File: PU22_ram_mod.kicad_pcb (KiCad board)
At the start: 2 copper layers, 39.2 x 94.7 mm, 11 parts, among them J1 MOBO, J2 BA8, J3 BA10

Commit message: Tweaked traces a bit
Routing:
- net /D25: track 96.8 -> 91.1 mm
- net /D26: track 97.5 -> 92.2 mm
- net /D27: track 98.2 -> 93.7 mm
- net /D28: track 93.0 -> 89.6 mm
- net /D29: track 92.0 -> 89.5 mm
- net /D30: track 91.3 -> 89.4 mm
- net /D3: track 94.5 -> 94.0 mm

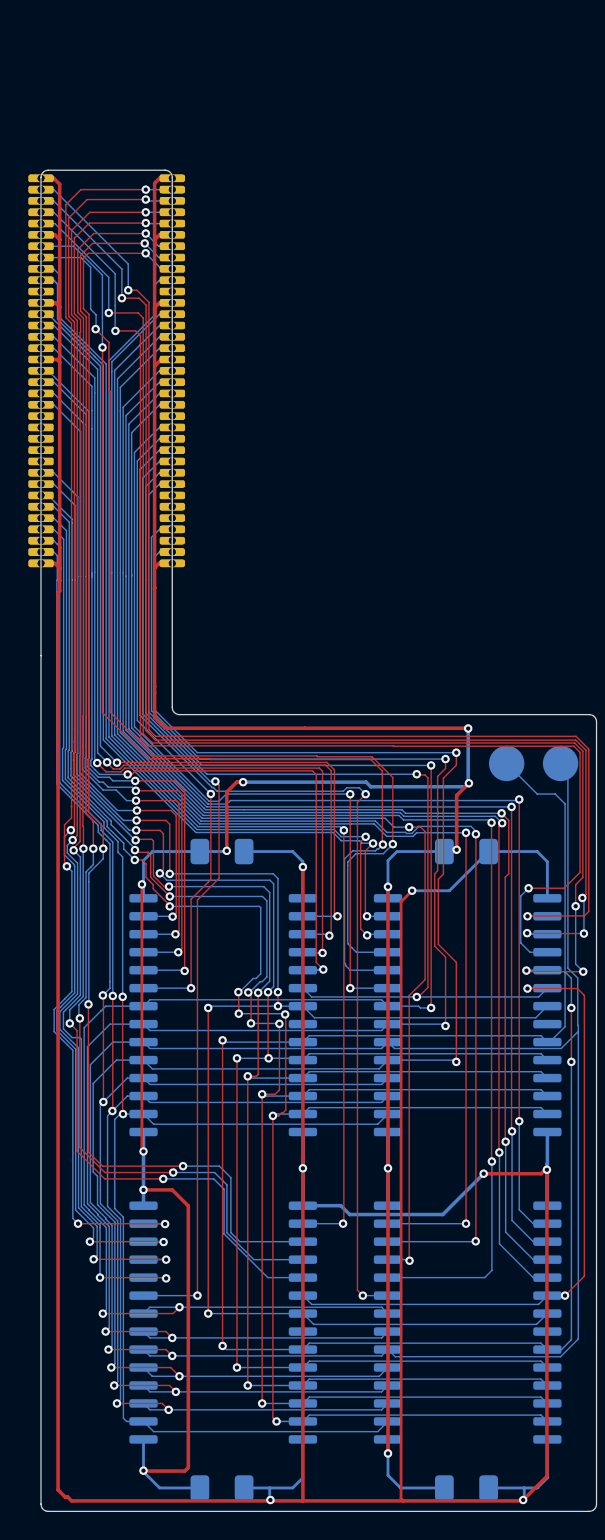
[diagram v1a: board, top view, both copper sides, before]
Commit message: make PCB a bit longer
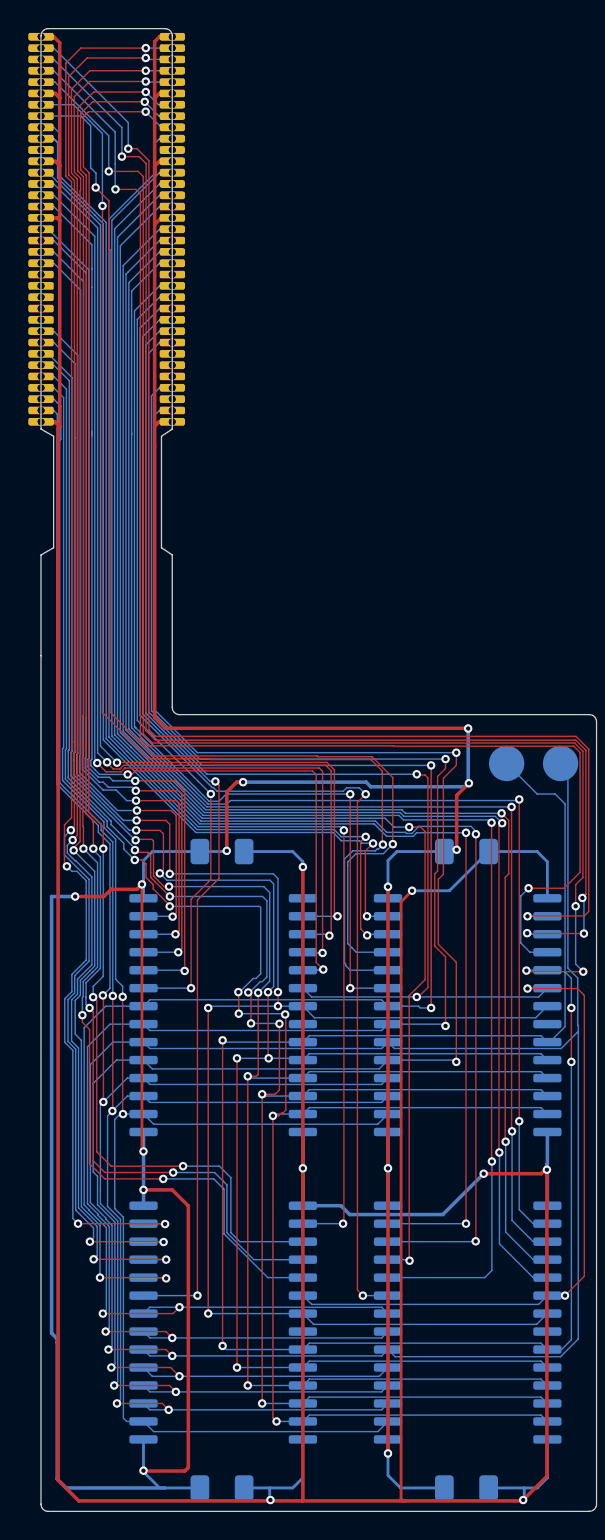
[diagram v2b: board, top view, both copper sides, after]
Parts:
- moved J1 10.0 mm to (117.0, 39.3)
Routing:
- net GND: track 224.2 -> 290.1 mm, vias 12 -> 13
- net /D31: track 89.8 -> 100.2 mm
- net /D30: track 89.4 -> 99.6 mm
- net /D29: track 89.5 -> 99.7 mm
- net /~{CAS1}: track 56.8 -> 66.9 mm
- net /D26: track 92.2 -> 102.3 mm
- net /A2: track 119.7 -> 129.8 mm
- net /D27: track 93.7 -> 103.7 mm
- net /A0: track 120.4 -> 130.4 mm
- net /~{WE}: track 120.2 -> 130.2 mm
- net /D17: track 87.2 -> 97.2 mm
- net /A6: track 105.7 -> 115.7 mm
- net /~{RAS}: track 122.1 -> 132.1 mm
- net /D3: track 94.0 -> 104.0 mm
- net /D23: track 93.3 -> 103.3 mm
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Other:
- board size 39.2 x 94.7 mm -> 39.2 x 104.7 mm

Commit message: Change outline
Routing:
- net GND: track 290.1 -> 296.2 mm, vias 13 -> 14
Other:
- board size 39.2 x 104.7 mm -> 39.1 x 104.6 mm

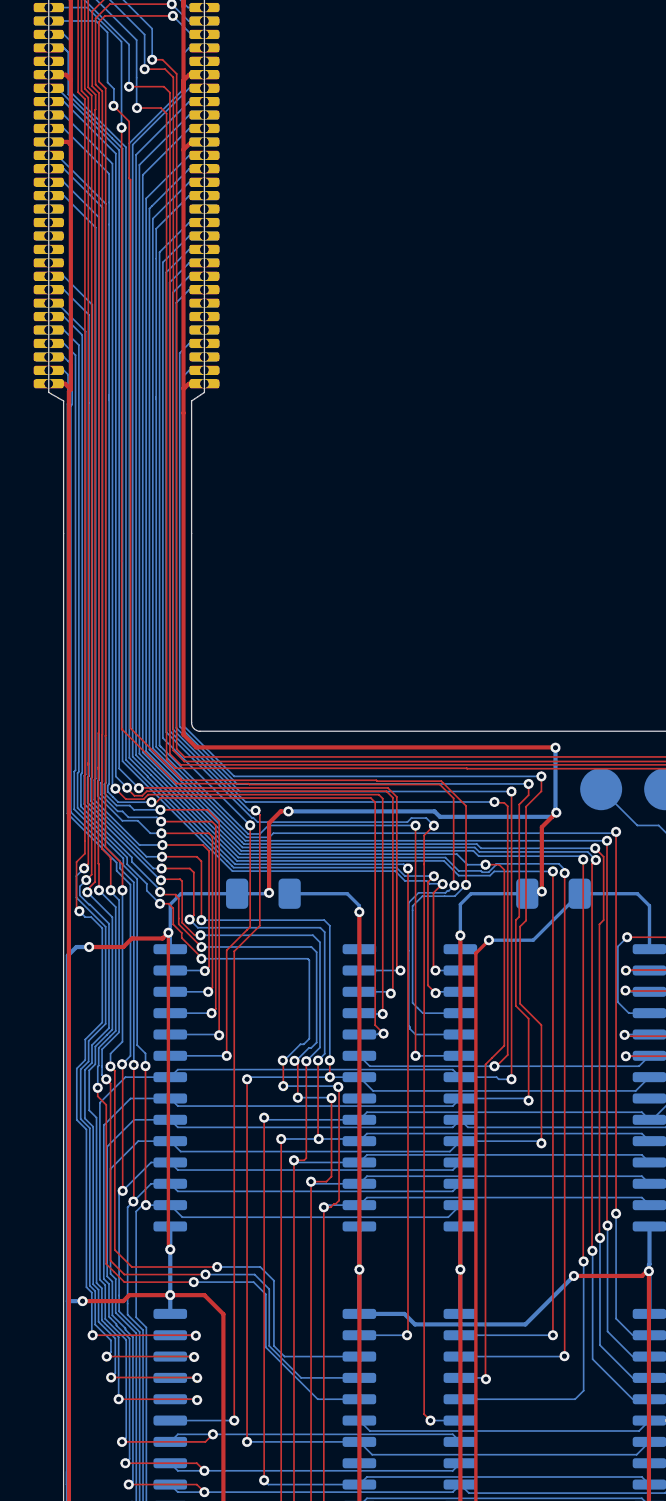
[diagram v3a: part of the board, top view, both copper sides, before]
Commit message: Reroute traces
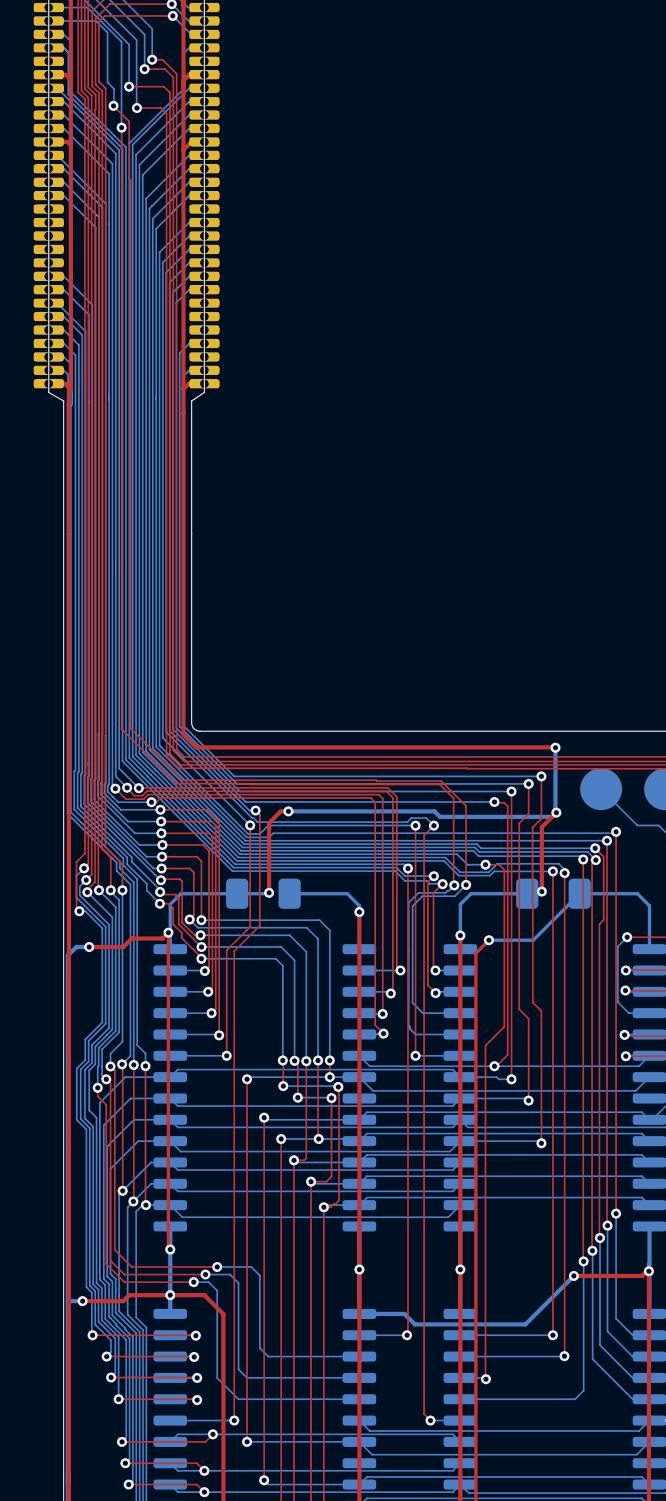
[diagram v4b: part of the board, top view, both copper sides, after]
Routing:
- net /A3: track 129.1 -> 126.5 mm
- net /A2: track 129.8 -> 127.5 mm
- net /A1: track 129.0 -> 127.5 mm
- net /D27: track 103.7 -> 104.8 mm
- net /D26: track 102.3 -> 103.3 mm
- net /A0: track 130.4 -> 129.6 mm
- net /A7: track 138.2 -> 137.6 mm

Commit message: More routing
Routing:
- net /D4: track 86.7 -> 89.2 mm
- net /D5: track 85.0 -> 86.0 mm
- net /D25: track 100.7 -> 100.2 mm

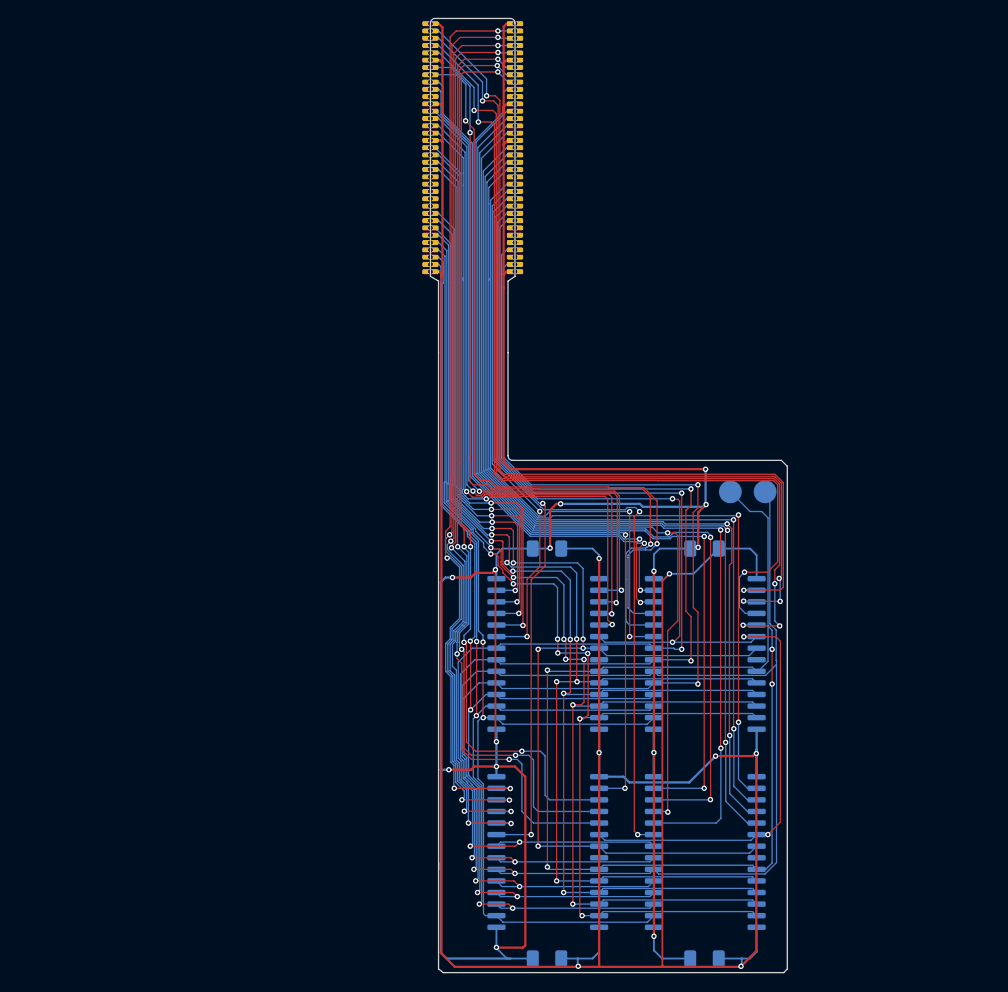
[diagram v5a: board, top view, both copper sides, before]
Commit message: Add copper fill in the zone with RAMs
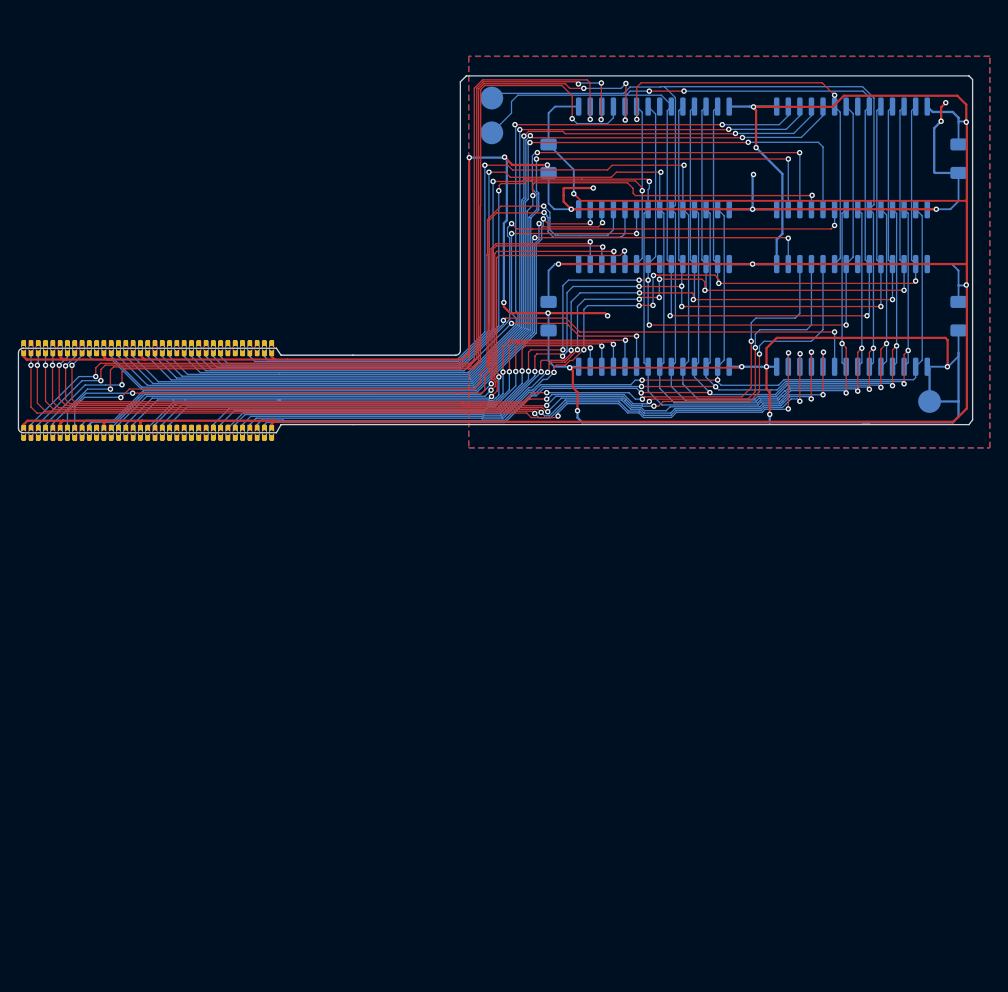
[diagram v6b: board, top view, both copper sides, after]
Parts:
- added J4: GND, TestPoint:TestPoint_Pad_D2.5mm, B.Cu at (171.7, 80.8)
- moved C2 92.0 mm to (174.9, 54.1), turned to -90 degrees
- moved C1 83.7 mm to (174.9, 71.4), turned to -90 degrees
- moved U3 73.5 mm to (154.9, 48.4), turned to -90 degrees
- moved J1 63.3 mm to (72.4, 84.2), turned to 90 degrees
- moved U4 59.5 mm to (154.9, 65.7), turned to -90 degrees
- moved U1 55.3 mm to (133.2, 48.4), turned to -90 degrees
- moved J2 52.6 mm to (123.7, 47.5), turned to -90 degrees
- moved J3 47.3 mm to (123.7, 51.3), turned to -90 degrees
- moved C4 46.0 mm to (129.9, 54.1), turned to -90 degrees
- moved U2 34.6 mm to (133.2, 65.7), turned to -90 degrees
- moved C3 25.5 mm to (129.9, 71.4), turned to -90 degrees
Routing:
- net GND: track 296.2 -> 330.6 mm, vias 14 -> 19
- net VCC: track 320.6 -> 322.5 mm
- net /D21: track 97.1 -> 97.9 mm
- added copper zone on B.Cu, net GND
- added copper zone on F.Cu, net GND
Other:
- board size 39.1 x 104.6 mm -> 104.6 x 39.1 mm

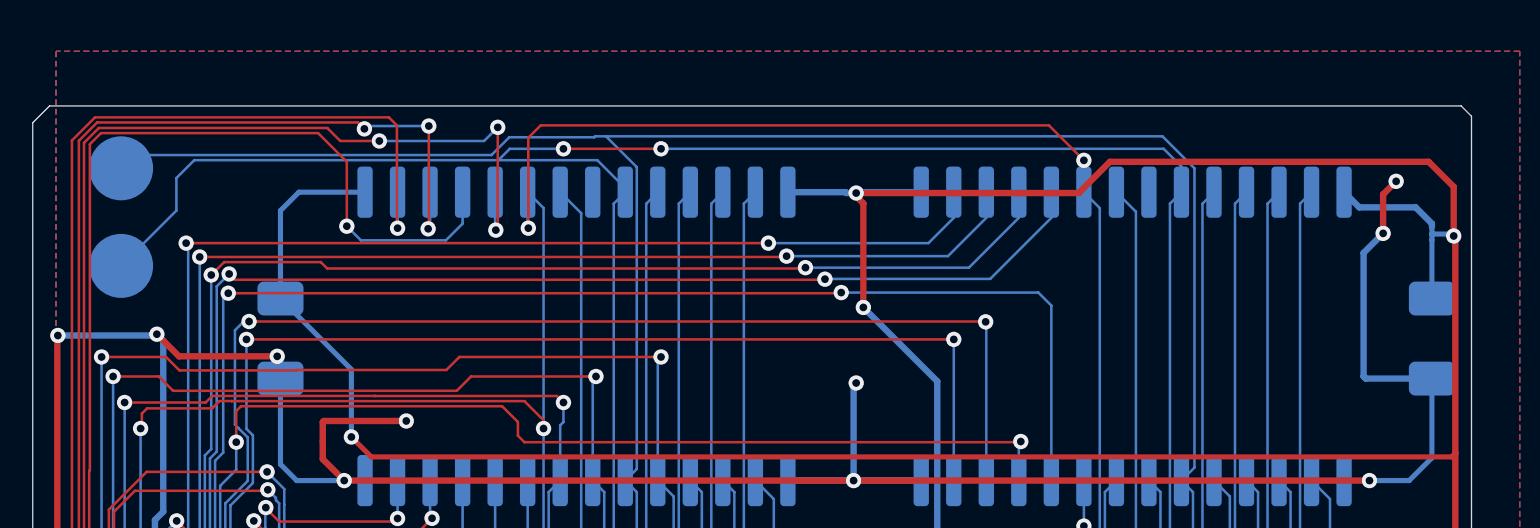
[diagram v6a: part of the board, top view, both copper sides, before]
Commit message: Some more ground plane
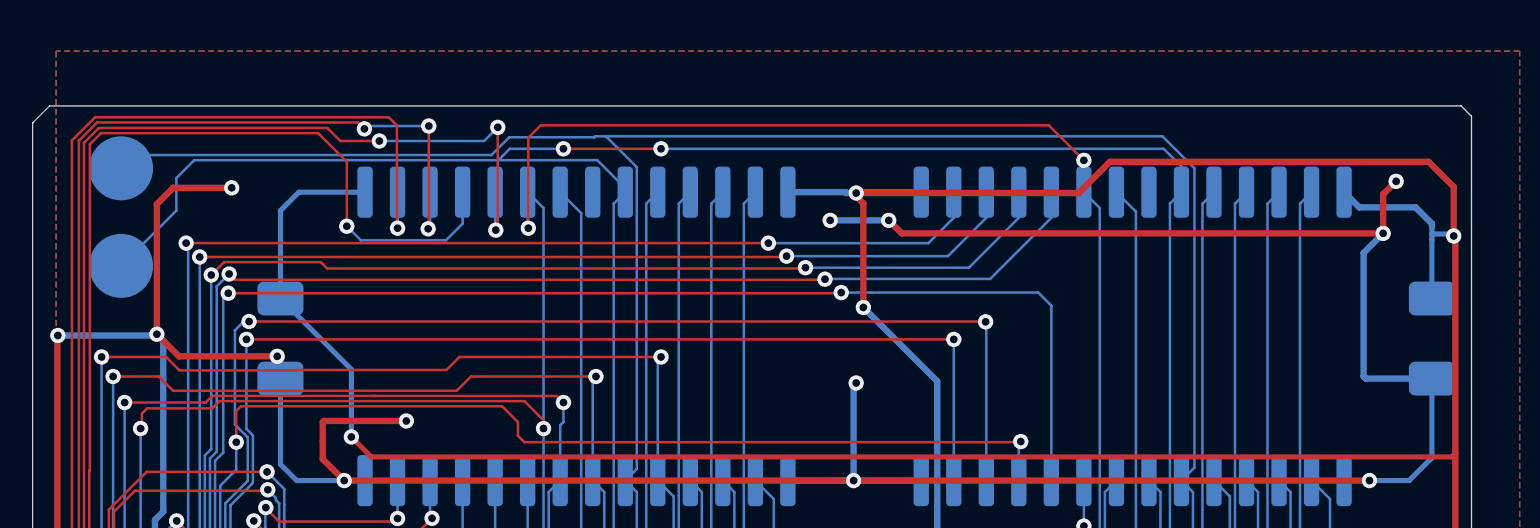
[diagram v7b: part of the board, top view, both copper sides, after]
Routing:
- net GND: track 330.6 -> 360.7 mm, vias 19 -> 22
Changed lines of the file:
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@@
 			(outputformat 1)
 			(mirror no)
-			(drillshape 1)
+			(drillshape 0)
 			(scaleselection 1)
-			(outputdirectory "")
+			(outputdirectory "gerbers/")
 		)
 	)
@@
 	)
 	(segment
+		(start 125.095 53.975)
+		(end 125.095 48.895)
+		(width 0.25)
+		(layer "F.Cu")
+		(net 2)
+	)
+	(segment
 		(start 81.16 75.829999)
 		(end 81.504601 76.1746)
@@
 	)
 	(segment
+		(start 125.476 48.514)
+		(end 125.73 48.26)
+		(width 0.25)
+		(layer "F.Cu")
+		(net 2)
+	)
+	(segment
+		(start 154.178 50.038)
+		(end 153.67 49.53)
+		(width 0.25)
+		(layer "F.Cu")
+		(net 2)
+	)
+	(segment
 		(start 101.2968 76.1746)
 		(end 120.4468 76.1746)
@@
 	)
 	(segment
+		(start 172.974 50.038)
+		(end 154.178 50.038)
+		(width 0.25)
+		(layer "F.Cu")
+		(net 2)
+	)
+	(segment
 		(start 132.4102 59.69)
 		(end 131.572 58.8518)
@@
 		(net 2)
 	)
+	(segment
+		(start 125.73 48.26)
+		(end 128.016 48.26)
+		(width 0.25)
+		(layer "F.Cu")
+		(net 2)
+	)
+	(segment
+		(start 125.095 48.895)
+		(end 125.476 48.514)
+		(width 0.25)
+		(layer "F.Cu")
+		(net 2)
+	)
 	(via
 		(at 129.794 54.8386)
@@
 	)
 	(via
+		(at 151.384 49.53)
+		(size 0.6)
+		(drill 0.3)
+		(layers "F.Cu" "B.Cu")
+		(net 2)
+	)
+	(via
 		(at 151.1046 76.962)
 		(size 0.6)
@@
 	)
 	(via
+		(at 153.67 49.53)
+		(size 0.6)
+		(drill 0.3)
+		(layers "F.Cu" "B.Cu")
+		(net 2)
+	)
+	(via
 		(at 129.8702 71.078)
 		(size 0.6)
@@
 	)
 	(via
+		(at 128.016 48.26)
+		(size 0.6)
+		(drill 0.3)
+		(layers "F.Cu" "B.Cu")
+		(net 2)
+	)
+	(via
 		(at 153.8224 76.962)
 		(size 0.6)
@@
 		(width 0.25)
 		(layer "B.Cu")
+		(net 2)
+	)
+	(segment
+		(start 153.67 49.53)
+		(end 151.384 49.53)
+		(width 0.25)
+		(layer "B.Cu")
